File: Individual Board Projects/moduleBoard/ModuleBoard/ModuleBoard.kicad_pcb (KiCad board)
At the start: 2 copper layers, 74 x 85.4 mm, 18 parts, among them IC1 MSPM0C1103SDGS20R, J1 Rotation Servo, J2 Extention Servo, J3 Debug, J4 5x2.54mm+2xBus, J5 5x2.54mm+2xBus, J6 5x2.54mm+2xBus, J7 5x2.54mm+2xBus, J8 5x2.54mm+2xBus, J9 5x2.54mm+2xBus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

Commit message: Module Layout Rev 0
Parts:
- C1, C2, C3, IC1, J1, J3, R1: moved to B.Cu
- moved J5 153.5 mm to (205.9, 117.9), turned to -60 degrees
- moved C4 152.8 mm to (206.1, 84.3), turned to 180 degrees
- moved C2 141.7 mm to (194.6, 73.2), turned to 90 degrees
- moved C3 140.3 mm to (192.9, 73.2), turned to -90 degrees
- moved C1 139.4 mm to (192.9, 78.4), turned to 180 degrees
- moved R1 134.4 mm to (193.2, 76.3)
- moved R3 134.3 mm to (190.2, 61.8), turned to 90 degrees
- moved J3 131.5 mm to (180.2, 75.9), turned to -90 degrees
- moved R2 131.5 mm to (188.0, 61.8), turned to 90 degrees
- moved J4 130.7 mm to (172.3, 117.9), turned to -120 degrees
- moved U1 128.0 mm to (203.5, 88.8), turned to 90 degrees
- moved J7 126.7 mm to (205.9, 59.7), turned to 60 degrees
- moved IC1 116.1 mm to (199.0, 75.7)
- moved J1 111.5 mm to (175.7, 79.9), turned to -90 degrees
- moved J6 102.2 mm to (172.3, 59.7), turned to 120 degrees
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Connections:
- net Net-(IC1-PA11) renamed /Extention Bottom Out
- net Net-(IC1-PA16_/_A8) renamed /Rotation Key
- C4 pad 2: +3.3V -> +5V
- IC1 pad 17: /nShoutIn1 -> /nShoutIn2
- IC1 pad 18: /nShoutIn2 -> /nShoutIn6
- IC1 pad 3: /nShoutIn6 -> /nShoutIn1
- U1 pad 3: +3.3V -> +5V
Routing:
- net /nShoutOut: track 0.00 -> 238.6 mm
- net /MSP TX: track 0.00 -> 238.2 mm
- net /MSP RX: track 0.00 -> 230.6 mm
- net +3.3V: track 0.00 -> 96.7 mm
- net /nShoutIn1: track 0.00 -> 91.1 mm
- net +5V: track 0.00 -> 66.2 mm
- net /nShoutIn4: track 0.00 -> 52.8 mm
- net /Linear Motor PWM: track 0.00 -> 50.6 mm
- net /nShoutIn5: track 0.00 -> 44.9 mm
- net /nShoutIn3: track 0.00 -> 43.4 mm
- net /Extention Bottom Out: track 0.00 -> 30.1 mm, vias 0 -> 1
- net /Rotary Motor PWM: track 0.00 -> 28.6 mm
- net /Rotation Key: track 0.00 -> 25.7 mm, vias 0 -> 1
- net /nShoutIn6: track 0.00 -> 25.4 mm
- net GND: track 0.00 -> 25.3 mm, vias 0 -> 4
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- added copper zone on F.Cu, net +3.3V
- added copper zone on B.Cu, net +5V
- added copper zone on F.Cu, net /Extention Bottom Out
- added copper zone on B.Cu, net GND
- added copper zone on F.Cu, net GND
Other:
- board text added: "5V Connector and Ideally GND will be tied together via auxilary cables soldered to the fuse points"
- board text added: "A trace rounding post process will be applied after this commit"
- board text added: "Excuse the absolutely atrochious routing, cross talk is fake."

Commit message: Interconnect Board
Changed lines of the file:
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@@
 	)
 	(segment
-		(start 198.6125 76.571529)
-		(end 199.354528 77.313559)
+		(start 197.77 73.41)
+		(end 198.6125 74.2525)
 		(width 0.2)
 		(layer "B.Cu")
@@
 	)
 	(segment
-		(start 196.847 73.469)
-		(end 197.829 73.469)
+		(start 199.354528 77.313559)
+		(end 199.354528 80.452371)
+		(width 0.2)
+		(layer "B.Cu")
+		(net 13)
+	)
+	(segment
+		(start 197.955009 81.85189)
+		(end 196.297324 81.85189)
+		(width 0.2)
+		(layer "B.Cu")
+		(net 13)
+	)
+	(segment
+		(start 195.946393 81.50096)
+		(end 182.33096 81.50096)
+		(width 0.2)
+		(layer "B.Cu")
+		(net 13)
+	)
+	(segment
+		(start 196.808 73.41)
+		(end 197.77 73.41)
+		(width 0.2)
+		(layer "B.Cu")
+		(net 13)
+	)
+	(segment
+		(start 182.33096 81.50096)
+		(end 180.75 79.92)
 		(width 0.2)
 		(layer "B.Cu")
@@
 	)
 	(segment
+		(start 198.6125 74.2525)
+		(end 198.6125 76.571529)
+		(width 0.2)
+		(layer "B.Cu")
+		(net 13)
+	)
+	(segment
+		(start 198.6125 76.571529)
+		(end 199.354528 77.313559)
+		(width 0.2)
+		(layer "B.Cu")
+		(net 13)
+	)
+	(segment
 		(start 199.354528 80.452371)
 		(end 197.955009 81.85189)
@@
 	)
 	(segment
-		(start 197.829 73.469)
-		(end 198.6125 74.2525)
+		(start 196.798 73.42)
+		(end 196.808 73.41)
 		(width 0.2)
 		(layer "B.Cu")
-		(net 13)
-	)
-	(segment
-		(start 198.6125 74.2525)
-		(end 198.6125 76.571529)
-		(width 0.2)
-		(layer "B.Cu")
-		(net 13)
-	)
-	(segment
-		(start 195.946393 81.50096)
-		(end 182.33096 81.50096)
-		(width 0.2)
-		(layer "B.Cu")
-		(net 13)
-	)
-	(segment
-		(start 197.955009 81.85189)
-		(end 196.297324 81.85189)
-		(width 0.2)
-		(layer "B.Cu")
-		(net 13)
-	)
-	(segment
-		(start 199.354528 77.313559)
-		(end 199.354528 80.452371)
-		(width 0.2)
-		(layer "B.Cu")
-		(net 13)
-	)
-	(segment
-		(start 182.33096 81.50096)
-		(end 180.75 79.92)
-		(width 0.2)
-		(layer "B.Cu")

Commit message: module mods
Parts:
- moved R2 11.0 mm to (192.3, 71.9), turned to 0 degrees
- moved R3 1.71 mm to (189.1, 60.5)
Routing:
- net /Extention Bottom Out: track 30.1 -> 25.6 mm
- net /Rotation Key: track 25.7 -> 22.2 mm
- net GND: track 25.3 -> 23.4 mm
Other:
- board text added: "G"

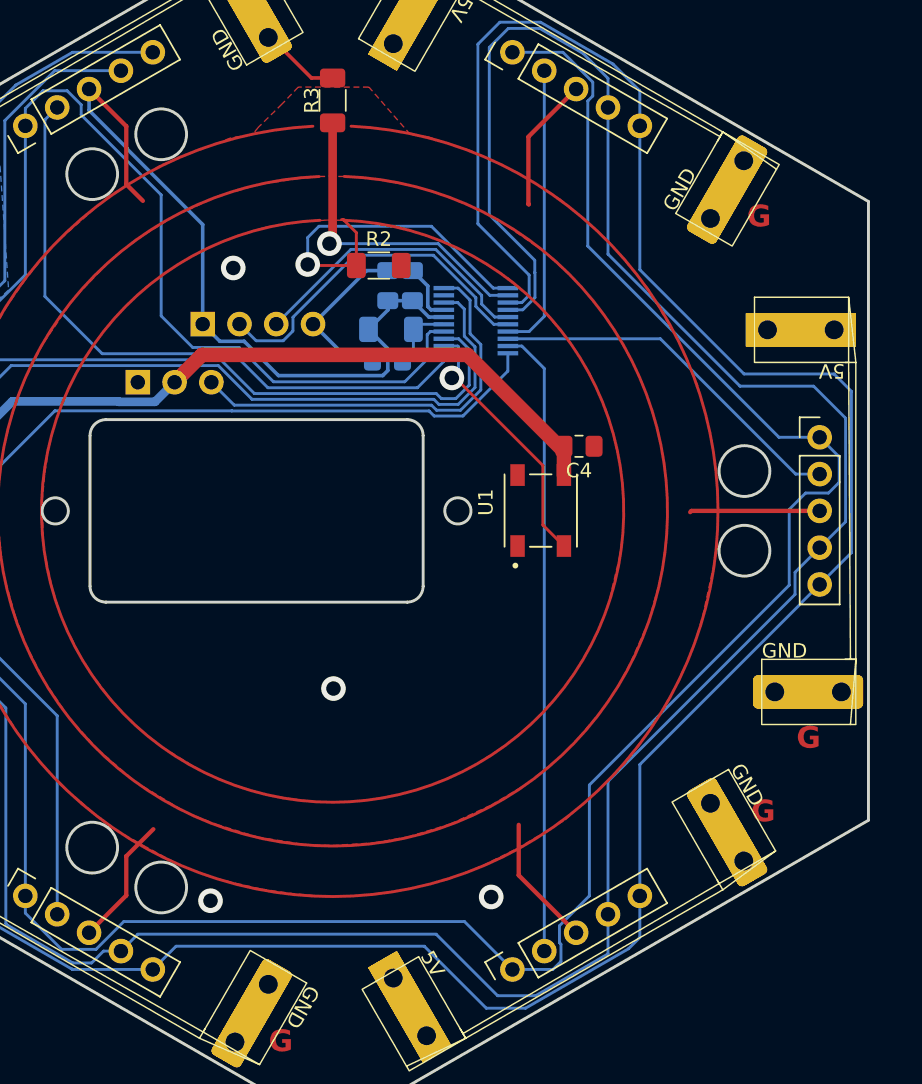
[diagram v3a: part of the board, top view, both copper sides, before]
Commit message: Gerbers For Interconnect And Module
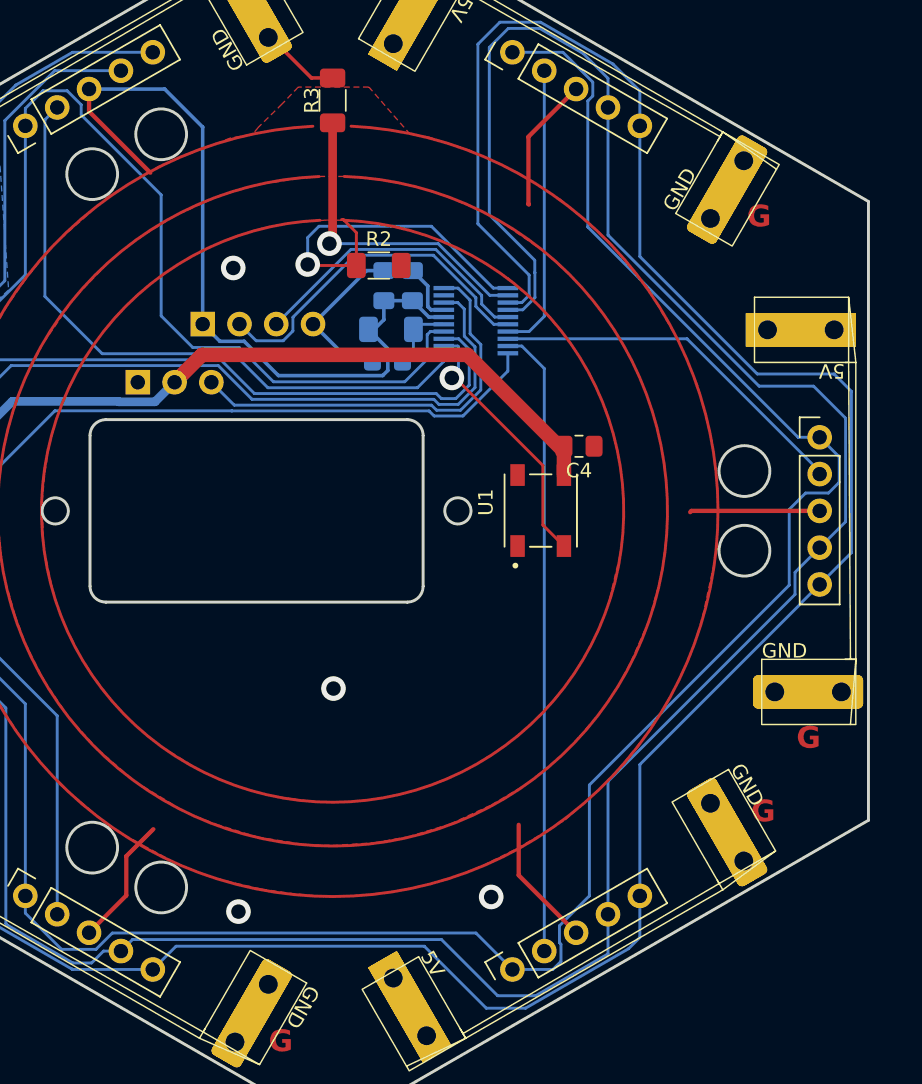
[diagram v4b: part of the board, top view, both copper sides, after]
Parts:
- moved C3 0.27 mm to (192.7, 73.2)
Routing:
- net +3.3V: track 96.7 -> 98.4 mm
- net /nShoutOut: track 238.6 -> 237.2 mm
- net /MSP RX: track 230.6 -> 229.6 mm
- net /MSP TX: track 238.2 -> 237.7 mm
